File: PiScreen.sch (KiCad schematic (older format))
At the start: 17 parts, among them P1 M02X05, P2 M02X05, P3 CONN_14, P4 CONN_5, P5 CONN_5, P6 CONN_5

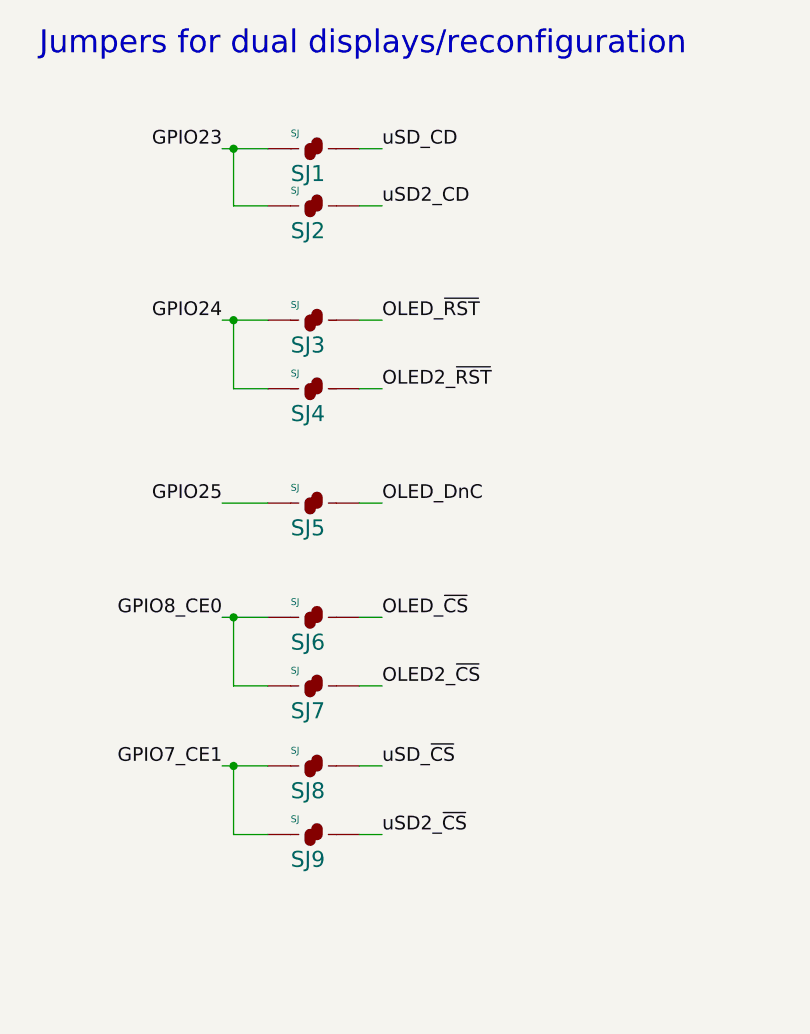
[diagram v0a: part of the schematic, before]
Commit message: Fix SJ8 & SJ9 to be open by default (screen connecting to SPI CE0 not CE1)
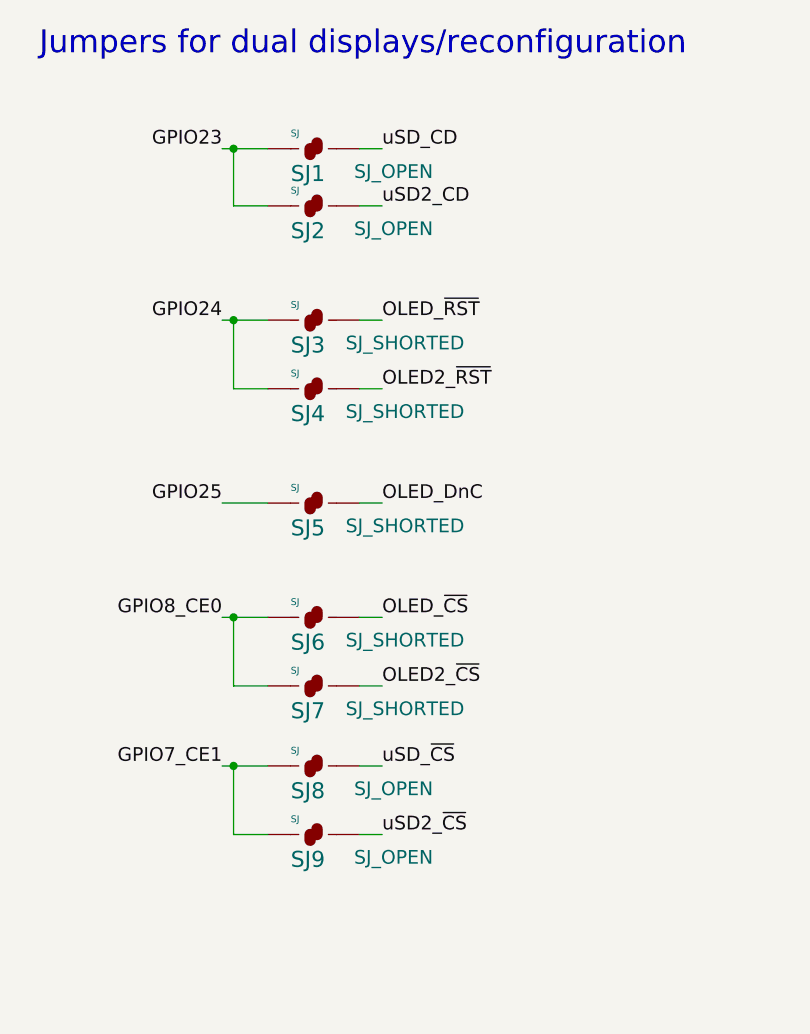
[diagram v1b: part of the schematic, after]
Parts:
- JP1: footprint (none) -> pin_array_13x2
- P1, P2: footprint ~ -> DIL10
- P3: footprint (none) -> 1X14
- P4, P5, P6: footprint (none) -> 1X05
- R1: footprint (none) -> SM0603_Resistor
- SJ1, SJ2, SJ8, SJ9: footprint (none) -> SJ_OPEN
- SJ3, SJ4, SJ5, SJ6, SJ7: footprint (none) -> SJ_SHORTED
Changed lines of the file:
@@
 Sheet 1 1
 Title ""
-Date ""
+Date "12 feb 2014"
 Rev ""
 Comp ""
@@
 F 0 "P1" H 9700 2500 50  0000 C CNN
 F 1 "M02X05" H 9750 1900 40  0000 C CNN
-F 2 "~" H 9800 2400 60  0000 C CNN
+F 2 "DIL10" H 9800 2400 60  0001 C CNN
 F 3 "~" H 9800 2400 60  0000 C CNN
 	1    9800 2400
@@
 F 0 "R1" V 10230 3050 40  0000 C CNN
 F 1 "47K" V 10157 3051 40  0000 C CNN
-F 2 "" V 10080 3050 30  0000 C CNN
+F 2 "SM0603_Resistor" V 10080 3050 30  0001 C CNN
 F 3 "" H 10150 3050 30  0000 C CNN
 	1    10150 3050
@@
 F 0 "JP1" H 2400 2550 50  0000 C CNN
 F 1 "M02X13" H 2450 1150 40  0000 C CNN
-F 2 "" H 2500 2450 60  0000 C CNN
+F 2 "pin_array_13x2" H 2500 2450 60  0001 C CNN
 F 3 "" H 2500 2450 60  0000 C CNN
 	1    2500 2450
@@
 F 0 "P2" H 9700 4100 50  0000 C CNN
 F 1 "M02X05" H 9750 3500 40  0000 C CNN
-F 2 "~" H 9800 4000 60  0000 C CNN
+F 2 "DIL10" H 9800 4000 60  0001 C CNN
 F 3 "~" H 9800 4000 60  0000 C CNN
 	1    9800 4000
@@
 F 0 "SJ1" H 5900 2050 70  0000 L BNN
 F 1 "SJ" H 5900 2250 30  0000 L BNN
-F 2 "" H 6000 2200 60  0000 C CNN
+F 2 "SJ_OPEN" H 6350 2100 60  0000 C CNN
 F 3 "" H 6000 2200 60  0000 C CNN
 	1    6000 2200
@@
 F 0 "SJ2" H 5900 2300 70  0000 L BNN
 F 1 "SJ" H 5900 2500 30  0000 L BNN
-F 2 "" H 6000 2450 60  0000 C CNN
+F 2 "SJ_OPEN" H 6350 2350 60  0000 C CNN
 F 3 "" H 6000 2450 60  0000 C CNN
 	1    6000 2450
@@
 F 0 "SJ3" H 5900 2800 70  0000 L BNN
 F 1 "SJ" H 5900 3000 30  0000 L BNN
-F 2 "" H 6000 2950 60  0000 C CNN
+F 2 "SJ_SHORTED" H 6400 2850 60  0000 C CNN
 F 3 "" H 6000 2950 60  0000 C CNN
 	1    6000 2950
@@
 F 0 "SJ4" H 5900 3100 70  0000 L BNN
 F 1 "SJ" H 5900 3300 30  0000 L BNN
-F 2 "" H 6000 3250 60  0000 C CNN
+F 2 "SJ_SHORTED" H 6400 3150 60  0000 C CNN
 F 3 "" H 6000 3250 60  0000 C CNN
 	1    6000 3250
@@
 F 0 "SJ5" H 5900 3600 70  0000 L BNN
 F 1 "SJ" H 5900 3800 30  0000 L BNN
-F 2 "" H 6000 3750 60  0000 C CNN
+F 2 "SJ_SHORTED" H 6400 3650 60  0000 C CNN
 F 3 "" H 6000 3750 60  0000 C CNN
 	1    6000 3750
@@
 F 0 "SJ6" H 5900 4100 70  0000 L BNN
 F 1 "SJ" H 5900 4300 30  0000 L BNN
-F 2 "" H 6000 4250 60  0000 C CNN
+F 2 "SJ_SHORTED" H 6400 4150 60  0000 C CNN
 F 3 "" H 6000 4250 60  0000 C CNN
 	1    6000 4250
@@
 F 0 "SJ7" H 5900 4400 70  0000 L BNN
 F 1 "SJ" H 5900 4600 30  0000 L BNN
-F 2 "" H 6000 4550 60  0000 C CNN
+F 2 "SJ_SHORTED" H 6400 4450 60  0000 C CNN
 F 3 "" H 6000 4550 60  0000 C CNN
 	1    6000 4550
@@
 F 0 "SJ8" H 5900 4750 70  0000 L BNN
 F 1 "SJ" H 5900 4950 30  0000 L BNN
-F 2 "" H 6000 4900 60  0000 C CNN
+F 2 "SJ_OPEN" H 6350 4800 60  0000 C CNN
 F 3 "" H 6000 4900 60  0000 C CNN
 	1    6000 4900
@@
 F 0 "SJ9" H 5900 5050 70  0000 L BNN
 F 1 "SJ" H 5900 5250 30  0000 L BNN
-F 2 "" H 6000 5200 60  0000 C CNN
+F 2 "SJ_OPEN" H 6350 5100 60  0000 C CNN
 F 3 "" H 6000 5200 60  0000 C CNN
 	1    6000 5200
@@
 F 0 "P3" V 9620 5750 60  0000 C CNN
 F 1 "CONN_14" V 9730 5750 60  0000 C CNN
-F 2 "" H 9650 5750 60  0000 C CNN
+F 2 "1X14" H 9650 5750 60  0001 C CNN
 F 3 "" H 9650 5750 60  0000 C CNN
 	1    9650 5750
@@
 F 0 "P4" V 10650 5350 50  0000 C CNN
 F 1 "CONN_5" V 10750 5350 50  0000 C CNN
-F 2 "" H 10700 5350 60  0000 C CNN
+F 2 "1X05" H 10700 5350 60  0001 C CNN
 F 3 "" H 10700 5350 60  0000 C CNN
 	1    10700 5350
@@
 F 0 "P5" V 10650 5950 50  0000 C CNN
 F 1 "CONN_5" V 10750 5950 50  0000 C CNN
-F 2 "" H 10700 5950 60  0000 C CNN
+F 2 "1X05" H 10700 5950 60  0001 C CNN
 F 3 "" H 10700 5950 60  0000 C CNN
 	1    10700 5950
@@
 F 0 "P6" V 10650 6500 50  0000 C CNN
 F 1 "CONN_5" V 10750 6500 50  0000 C CNN
-F 2 "" H 10700 6500 60  0000 C CNN
+F 2 "1X05" H 10700 6500 60  0001 C CNN
 F 3 "" H 10700 6500 60  0000 C CNN
 	1    10700 6500
